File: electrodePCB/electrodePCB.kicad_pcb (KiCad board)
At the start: 2 copper layers, 58 x 58 mm, 20 parts, among them J1 FPC 20p, J2 qwiic, U1 TMP119AIYBGR

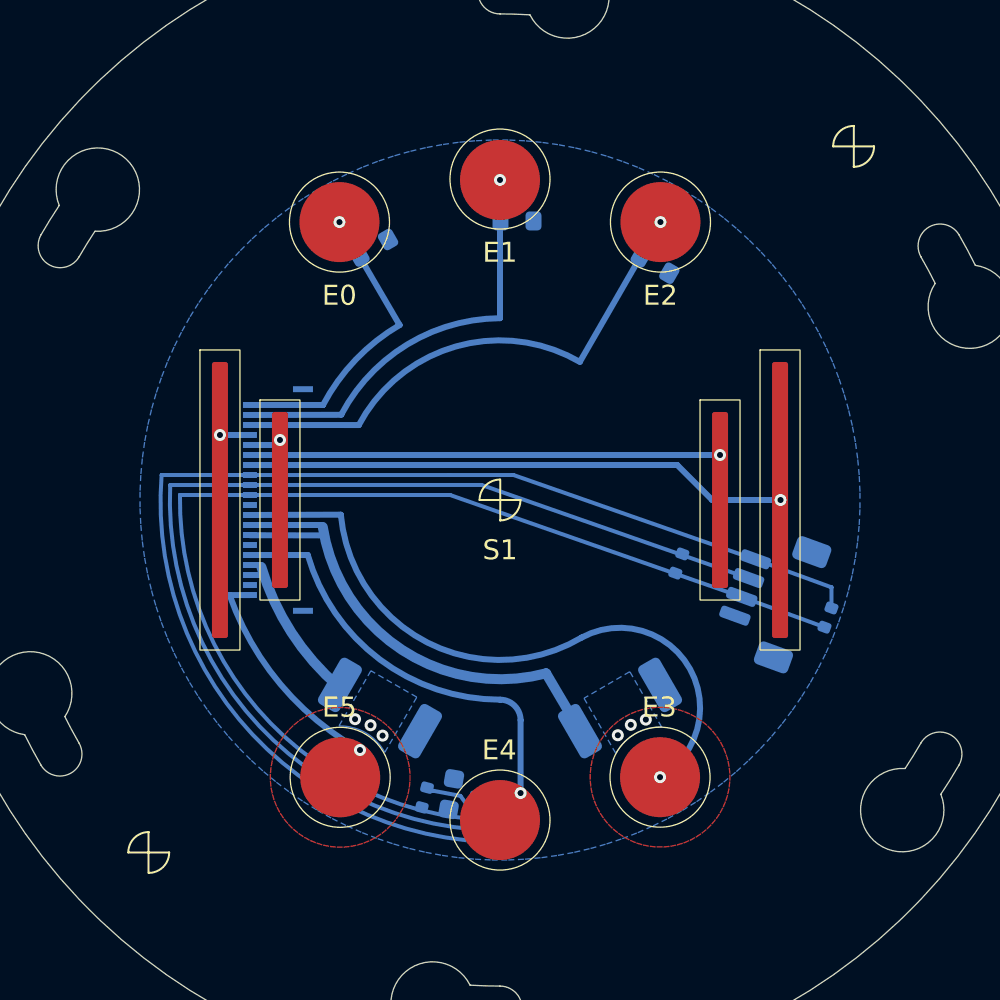
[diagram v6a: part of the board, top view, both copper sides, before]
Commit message: cleaning up GND plane and adapted thermal pads to have larger internal radius for fab flexibility.
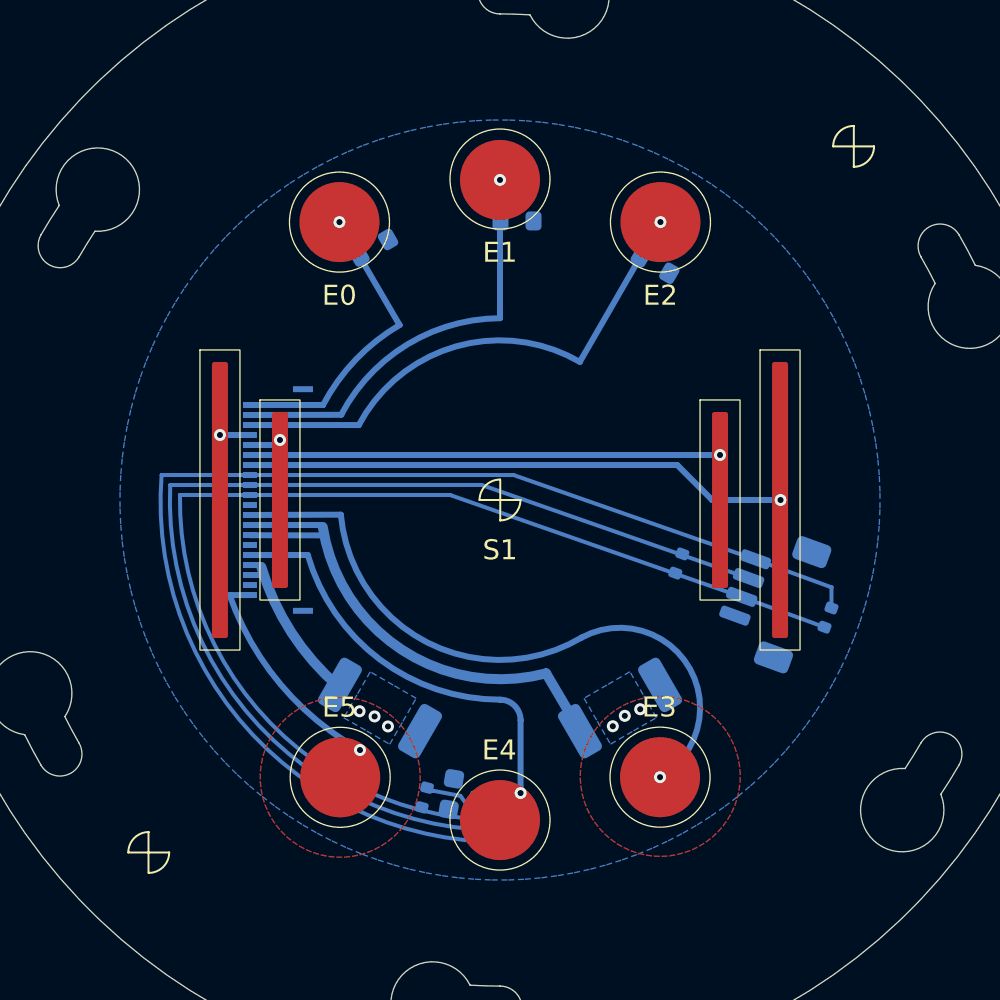
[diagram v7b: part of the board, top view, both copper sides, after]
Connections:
- J2 pad MP: unconnected-(J2-MountPin-PadMP) -> GND
